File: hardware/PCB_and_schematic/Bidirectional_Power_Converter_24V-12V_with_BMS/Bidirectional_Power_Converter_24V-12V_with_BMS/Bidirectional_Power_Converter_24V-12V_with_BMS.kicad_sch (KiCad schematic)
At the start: 1 part

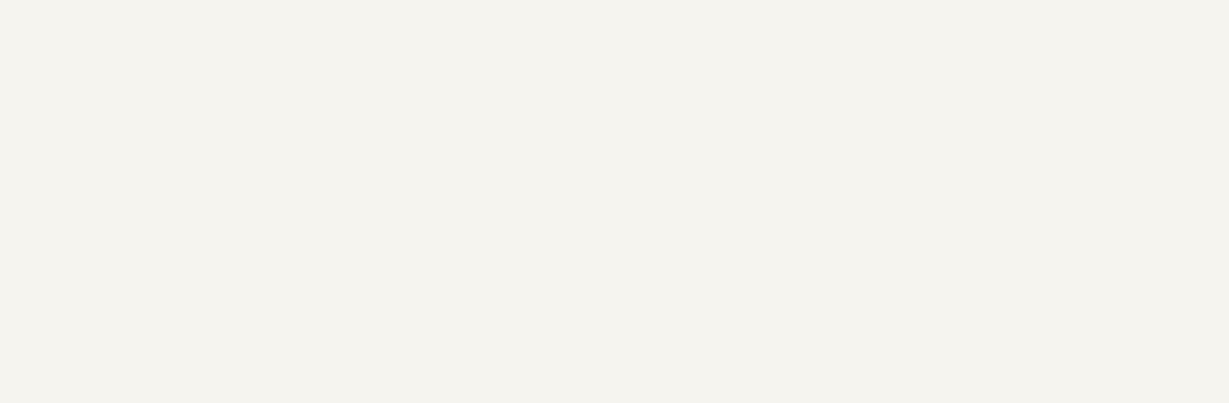
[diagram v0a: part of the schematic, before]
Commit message: Add first concept of tl494 power supply
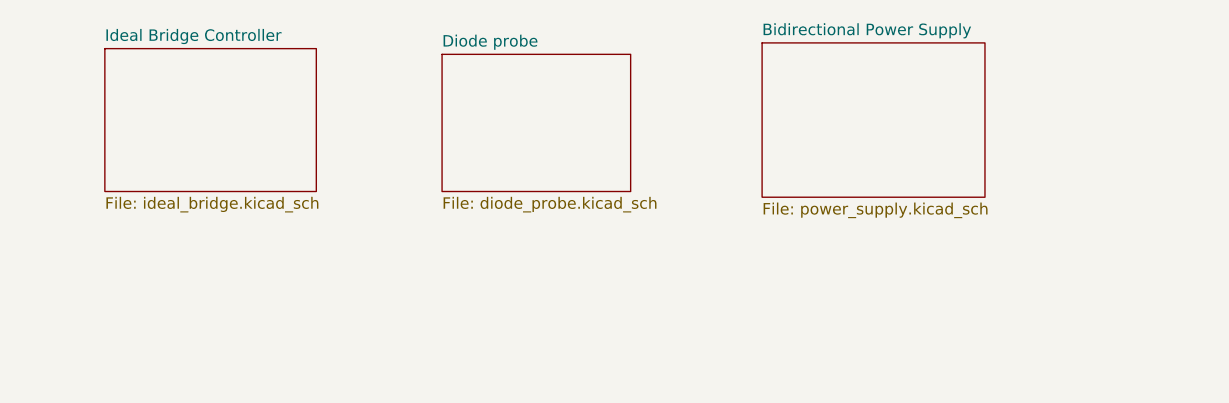
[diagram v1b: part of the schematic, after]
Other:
- added sheet Bidirectional Power Supply (power_supply.kicad_sch)
- added sheet Diode probe (diode_probe.kicad_sch)
- added sheet Ideal Bridge Controller (ideal_bridge.kicad_sch)
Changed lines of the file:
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@@
 		(exclude_from_sim no)
 		(in_bom yes)
-		(on_board yes)
+		(on_board no)
 		(dnp no)
 		(fields_autoplaced yes)
@@
 				)
 			)
+		)
+	)
+	(sheet
+		(at 74.295 20.955)
+		(size 20.955 15.24)
+		(fields_autoplaced yes)
+		(stroke
+			(width 0.1524)
+			(type solid)
+		)
+		(fill
+			(color 0 0 0 0.0000)
+		)
+		(property "Sheetname" "Diode probe"
+			(at 74.295 20.2434 0)
+			(effects
+				(font
+					(size 1.27 1.27)
+				)
+				(justify left bottom)
+			)
+		)
+		(property "Sheetfile" "diode_probe.kicad_sch"
+			(at 74.295 36.7796 0)
+			(effects
+				(font
+					(size 1.27 1.27)
+				)
+				(justify left top)
+			)
+		)
+		(instances
+			(project "Bidirectional_Power_Converter_24V-12V_with_BMS"
+				(path "/57ff2453-26d1-489b-aa83-9af273df178f"
+					(page "3")
+				)
+			)
+		)
+	)
+	(sheet
+		(at 109.855 19.685)
+		(size 24.765 17.145)
+		(fields_autoplaced yes)
+		(stroke
+			(width 0.1524)
+			(type solid)
+		)
+		(fill
+			(color 0 0 0 0.0000)
+		)
+		(property "Sheetname" "Bidirectional Power Supply"
+			(at 109.855 18.9734 0)
+			(effects
+				(font
+					(size 1.27 1.27)
+				)
+				(justify left bottom)
+			)
+		)
+		(property "Sheetfile" "power_supply.kicad_sch"
+			(at 109.855 37.4146 0)
+			(effects
+				(font
+					(size 1.27 1.27)
+				)
+				(justify left top)
+			)
+		)
+		(instances
+			(project "Bidirectional_Power_Converter_24V-12V_with_BMS"
+				(path "/57ff2453-26d1-489b-aa83-9af273df178f"
+					(page "4")
+				)
+			)
+		)
+	)
+	(sheet
+		(at 36.83 20.32)
+		(size 23.495 15.875)
+		(fields_autoplaced yes)
+		(stroke
+			(width 0.1524)
+			(type solid)
+		)
+		(fill
+			(color 0 0 0 0.0000)
+		)
+		(property "Sheetname" "Ideal Bridge Controller"
+			(at 36.83 19.6084 0)
+			(effects
+				(font
+					(size 1.27 1.27)
+				)
+				(justify left bottom)
+			)
+		)
+		(property "Sheetfile" "ideal_bridge.kicad_sch"
+			(at 36.83 36.7796 0)
+			(effects
+				(font
+					(size 1.27 1.27)
+				)
+				(justify left top)
+			)
+		)
+		(instances
+			(project "Bidirectional_Power_Converter_24V-12V_with_BMS"
+				(path "/57ff2453-26d1-489b-aa83-9af273df178f"
+					(page "2")
+				)
+			)

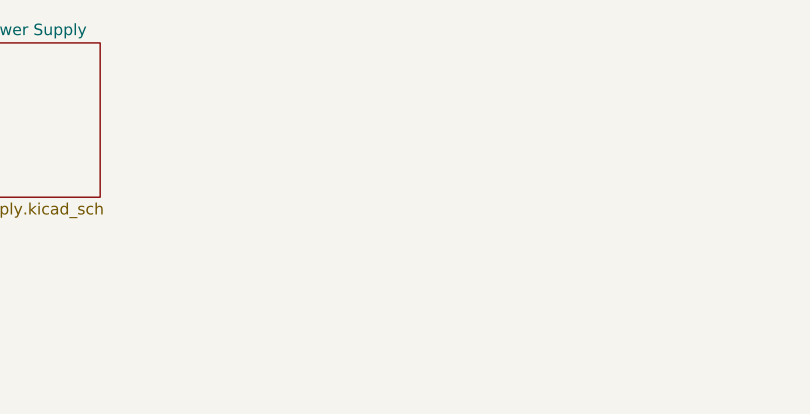
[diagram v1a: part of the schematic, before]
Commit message: Update schematic for ESP32, split schematic sheets
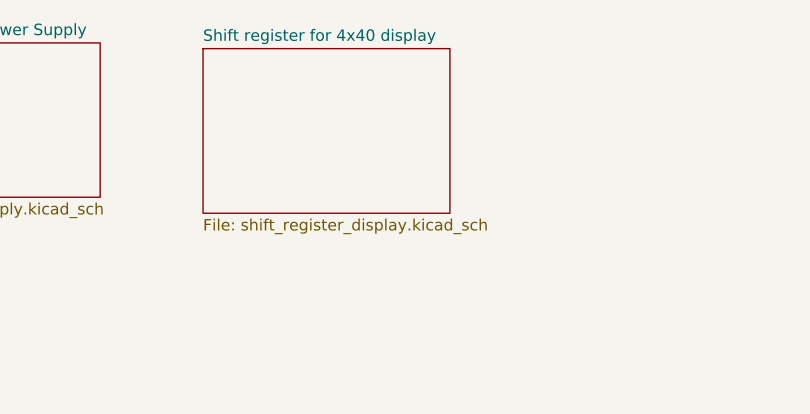
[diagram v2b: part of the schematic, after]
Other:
- added sheet Shift register for 4x40 display (shift_register_display.kicad_sch)
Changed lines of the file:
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@@
+	)
+	(sheet
+		(at 146.05 20.32)
+		(size 27.432 18.288)
+		(fields_autoplaced yes)
+		(stroke
+			(width 0.1524)
+			(type solid)
+		)
+		(fill
+			(color 0 0 0 0.0000)
+		)
+		(property "Sheetname" "Shift register for 4x40 display"
+			(at 146.05 19.6084 0)
+			(effects
+				(font
+					(size 1.27 1.27)
+				)
+				(justify left bottom)
+			)
+		)
+		(property "Sheetfile" "shift_register_display.kicad_sch"
+			(at 146.05 39.1926 0)
+			(effects
+				(font
+					(size 1.27 1.27)
+				)
+				(justify left top)
+			)
+		)
+		(instances
+			(project "Bidirectional_Power_Converter_24V-12V_with_BMS"
+				(path "/57ff2453-26d1-489b-aa83-9af273df178f"
+					(page "5")
+				)
+			)
+		)
 	)
 	(sheet

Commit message: Add bidirectional smps concept, split bms schematic
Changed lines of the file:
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@@
-	)
-	(rectangle
-		(start 104.14 83.058)
-		(end 146.558 110.49)
-		(stroke
-			(width 0)
-			(type default)
-		)
-		(fill
-			(type none)
-		)
 	)
 	(rectangle
@@
 	)
 	(sheet
-		(at 109.855 19.685)
-		(size 24.765 17.145)
+		(at 105.029 79.883)
+		(size 40.513 23.749)
 		(fields_autoplaced yes)
 		(stroke
@@
 		)
 		(property "Sheetname" "Bidirectional Power Supply"
-			(at 109.855 18.9734 0)
+			(at 105.029 79.1714 0)
 			(effects
 				(font
@@
 		)
 		(property "Sheetfile" "power_supply.kicad_sch"
-			(at 109.855 37.4146 0)
-			(effects
-				(font
+			(at 105.029 104.2166 0)
+			(effects
+				(font

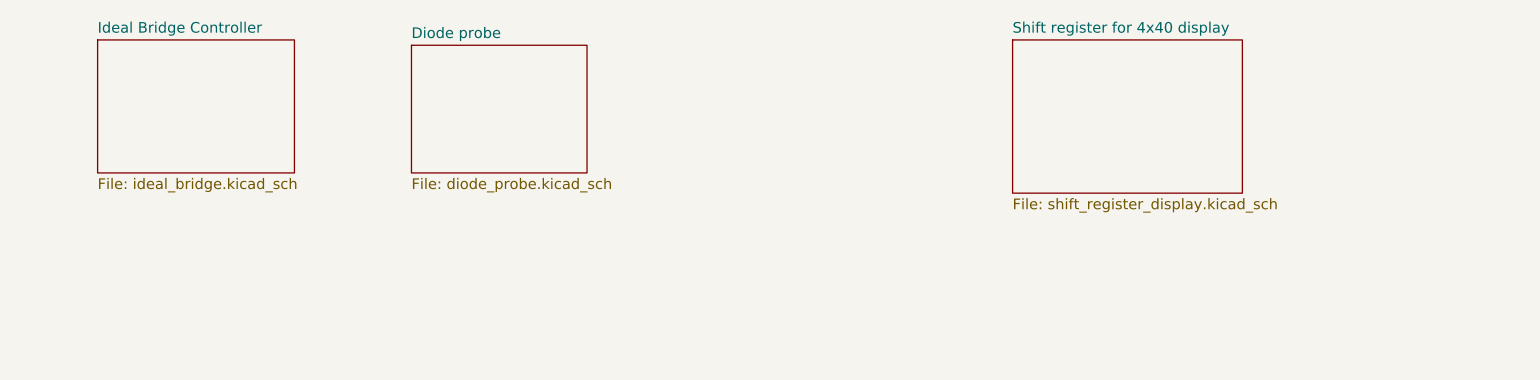
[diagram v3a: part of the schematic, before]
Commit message: Add misc shift register for display schematic, ideal bridge and sd card switcher
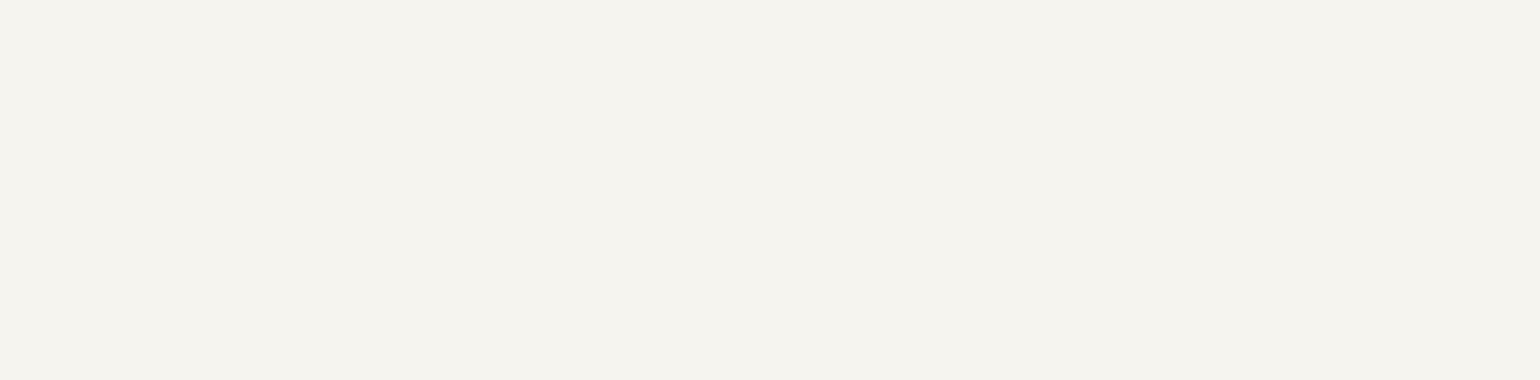
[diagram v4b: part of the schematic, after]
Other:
- removed sheet Diode probe
- removed sheet Ideal Bridge Controller
- removed sheet Shift register for 4x40 display
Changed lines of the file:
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@@
-	)
-	(sheet
-		(at 74.295 20.955)
-		(size 20.955 15.24)
-		(fields_autoplaced yes)
-		(stroke
-			(width 0.1524)
-			(type solid)
-		)
-		(fill
-			(color 0 0 0 0.0000)
-		)
-		(property "Sheetname" "Diode probe"
-			(at 74.295 20.2434 0)
-			(effects
-				(font
-					(size 1.27 1.27)
-				)
-				(justify left bottom)
-			)
-		)
-		(property "Sheetfile" "diode_probe.kicad_sch"
-			(at 74.295 36.7796 0)
-			(effects
-				(font
-					(size 1.27 1.27)
-				)
-				(justify left top)
-			)
-		)
-		(instances
-			(project "Bidirectional_Power_Converter_24V-12V_with_BMS"
-				(path "/57ff2453-26d1-489b-aa83-9af273df178f"
-					(page "3")
-				)
-			)
-		)
-	)
-	(sheet
-		(at 146.05 20.32)
-		(size 27.432 18.288)
-		(fields_autoplaced yes)
-		(stroke
-			(width 0.1524)
-			(type solid)
-		)
-		(fill
-			(color 0 0 0 0.0000)
-		)
-		(property "Sheetname" "Shift register for 4x40 display"
-			(at 146.05 19.6084 0)
-			(effects
-				(font
-					(size 1.27 1.27)
-				)
-				(justify left bottom)
-			)
-		)
-		(property "Sheetfile" "shift_register_display.kicad_sch"
-			(at 146.05 39.1926 0)
-			(effects
-				(font
-					(size 1.27 1.27)
-				)
-				(justify left top)
-			)
-		)
-		(instances
-			(project "Bidirectional_Power_Converter_24V-12V_with_BMS"
-				(path "/57ff2453-26d1-489b-aa83-9af273df178f"
-					(page "5")
-				)
-			)
-		)
 	)
 	(sheet
@@
 				)
 			)
-		)
-	)
-	(sheet
-		(at 36.83 20.32)
-		(size 23.495 15.875)
-		(fields_autoplaced yes)
-		(stroke
-			(width 0.1524)
-			(type solid)
-		)
-		(fill
-			(color 0 0 0 0.0000)
-		)
-		(property "Sheetname" "Ideal Bridge Controller"
-			(at 36.83 19.6084 0)
-			(effects
-				(font
-					(size 1.27 1.27)
-				)
-				(justify left bottom)
-			)
-		)
-		(property "Sheetfile" "ideal_bridge.kicad_sch"
-			(at 36.83 36.7796 0)
-			(effects
-				(font
-					(size 1.27 1.27)
-				)
-				(justify left top)
-			)
-		)
-		(instances
-			(project "Bidirectional_Power_Converter_24V-12V_with_BMS"
-				(path "/57ff2453-26d1-489b-aa83-9af273df178f"
-					(page "2")
-				)
-			)
